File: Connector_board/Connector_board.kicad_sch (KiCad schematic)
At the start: 7 parts, among them J1 SM03B-SRSS-TB, J2 USB_B_Micro, J3 Conn_02x07_Counter_Clockwise, J4 Conn_02x07_Odd_Even, J5 Conn_02x07_Counter_Clockwise

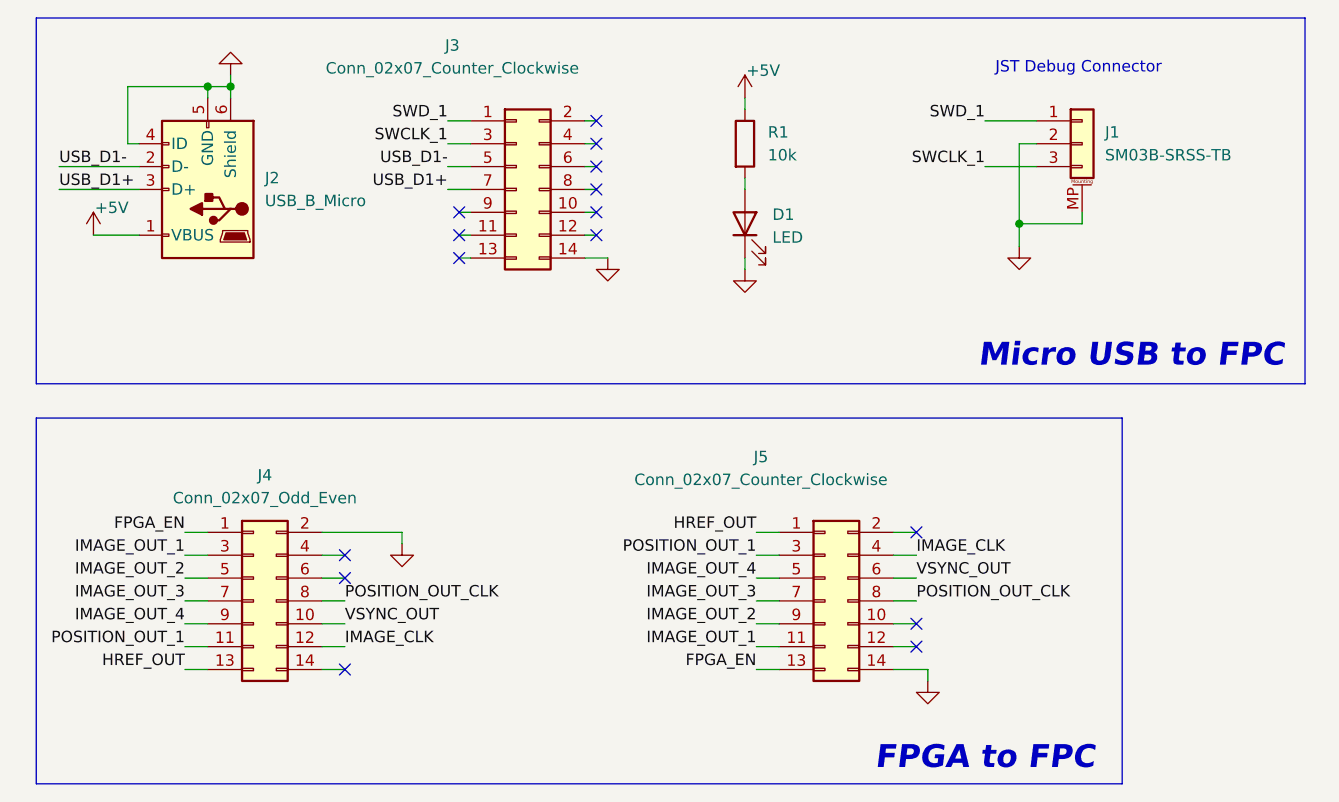
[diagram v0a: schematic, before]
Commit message: GPIO_1 added
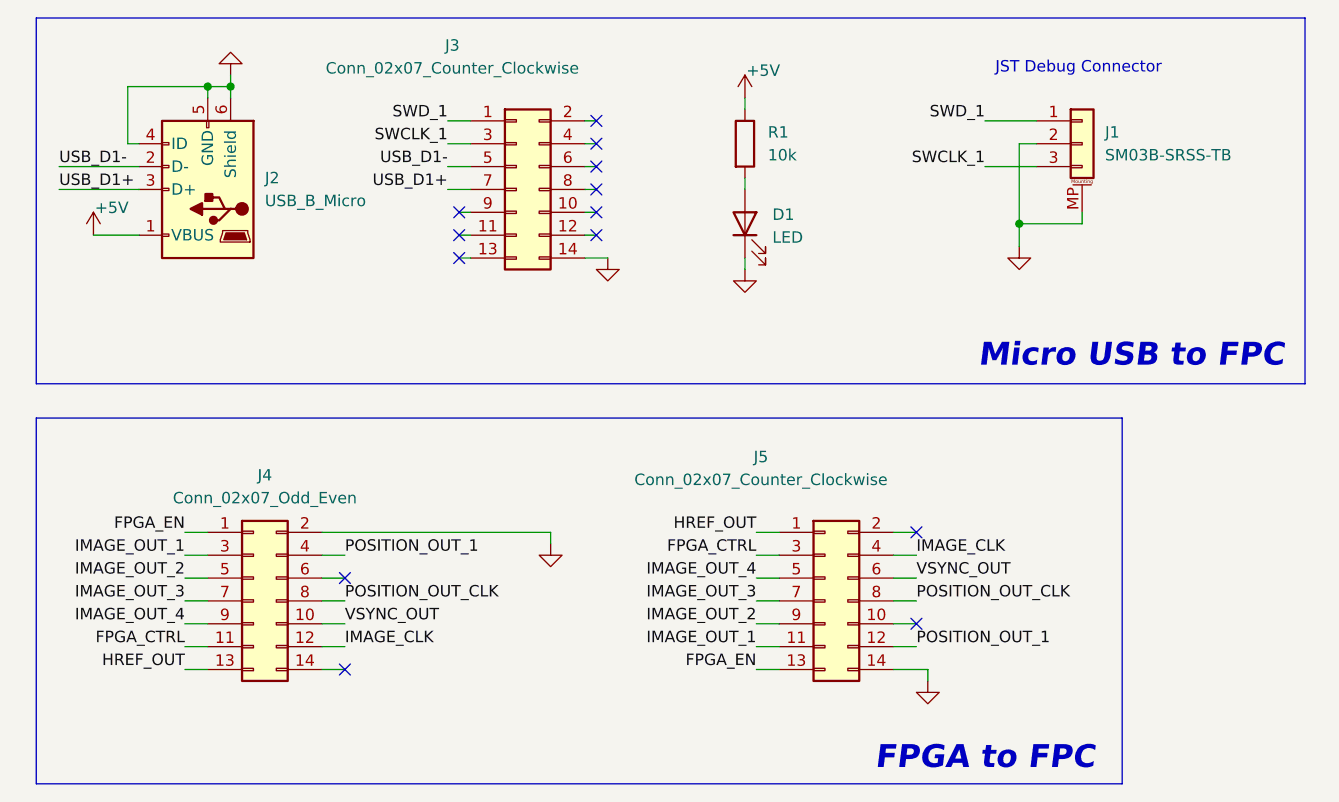
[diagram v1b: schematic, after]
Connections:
- net POSITION_OUT_1: now also J4.4 (Pin_4), J5.12 (Pin_12); no longer J4.11 (Pin_11), J5.3 (Pin_3)
- new net FPGA_CTRL: J4.11 (Pin_11), J5.3 (Pin_3)
- no-connect marks 15 -> 13
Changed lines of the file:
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@@
-	)
-	(no_connect
-		(at 111.76 83.82)
 	)
 	(no_connect
 		(at 60.96 35.56)
 	)
-	(no_connect
-		(at 48.26 73.66)
-	)
 	(wire
 		(pts
@@
 	(wire
 		(pts
-			(xy 45.72 71.12) (xy 54.61 71.12)
+			(xy 45.72 71.12) (xy 71.12 71.12)
 		)
 		(stroke
@@
 	(wire
 		(pts
-			(xy 54.61 72.39) (xy 54.61 71.12)
+			(xy 71.12 72.39) (xy 71.12 71.12)
 		)
 		(stroke
@@
 	)
 	(label "POSITION_OUT_1"
-		(at 30.48 83.82 180)
-		(effects
-			(font
-				(size 1.27 1.27)
-			)
-			(justify right bottom)
+		(at 111.76 83.82 0)
+		(effects
+			(font
+				(size 1.27 1.27)
+			)
+			(justify left bottom)
 		)
 	)
@@
 		)
 	)
+	(label "FPGA_CTRL"
+		(at 93.98 73.66 180)
+		(effects
+			(font
+				(size 1.27 1.27)
+			)
+			(justify right bottom)
+		)
+	)
+	(label "FPGA_CTRL"
+		(at 30.48 83.82 180)
+		(effects
+			(font
+				(size 1.27 1.27)
+			)
+			(justify right bottom)
+		)
+	)
 	(label "SWD_1"
 		(at 59.69 25.4 180)
@@
 		)
 	)
+	(label "POSITION_OUT_1"
+		(at 48.26 73.66 0)
+		(effects
+			(font
+				(size 1.27 1.27)
+			)
+			(justify left bottom)
+		)
+	)
 	(label "FPGA_EN"
 		(at 30.48 71.12 180)
@@
 	(label "IMAGE_OUT_3"
 		(at 93.98 78.74 180)
-		(effects
-			(font
-				(size 1.27 1.27)
-			)
-			(justify right bottom)
-		)
-	)
-	(label "POSITION_OUT_1"
-		(at 93.98 73.66 180)
 		(effects
 			(font
@@
 		(lib_name "GND_8")
 		(lib_id "power:GND")
-		(at 54.61 72.39 0)
+		(at 71.12 72.39 0)
 		(unit 1)
 		(body_style 1)
@@
 		(dnp no)
 		(property "Reference" "#PWR08"
-			(at 54.61 78.74 0)
+			(at 71.12 78.74 0)
 			(hide yes)
 			(show_name no)
@@
 		)
 		(property "Value" "GND"
-			(at 54.61 76.454 0)
+			(at 71.12 76.454 0)
 			(hide yes)
 			(show_name no)
@@
 		)
 		(property "Footprint" ""
-			(at 54.61 72.39 0)
+			(at 71.12 72.39 0)
 			(hide yes)
 			(show_name no)
@@
 		)
 		(property "Datasheet" ""
-			(at 54.61 72.39 0)
+			(at 71.12 72.39 0)
 			(hide yes)
 			(show_name no)
@@
 		)
 		(property "Description" "Power symbol creates a global label with name \"GND\" , ground"
-			(at 54.61 72.39 0)
-			(hide yes)
-			(show_name no)
+			(at 71.12 72.39 0)
+			(hide yes)
+			(show_name no)

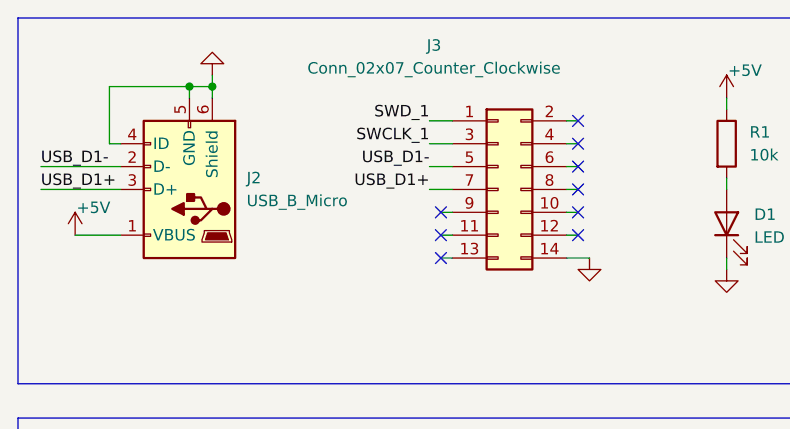
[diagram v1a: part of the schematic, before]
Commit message: connector board pin order updated
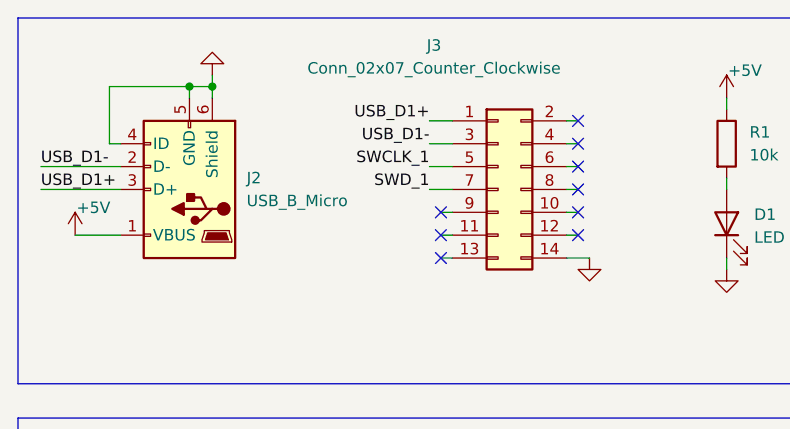
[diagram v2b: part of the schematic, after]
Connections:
- net SWCLK_1: now also J3.5 (Pin_5); no longer J3.3 (Pin_3)
- net SWD_1: now also J3.7 (Pin_7); no longer J3.1 (Pin_1)
- net USB_D1+: now also J3.1 (Pin_1); no longer J3.7 (Pin_7)
- net USB_D1-: now also J3.3 (Pin_3); no longer J3.5 (Pin_5)
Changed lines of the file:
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@@
+		)
+	)
+	(label "USB_D1+"
+		(at 59.69 25.4 180)
+		(effects
+			(font
+				(size 1.27 1.27)
+			)
+			(justify right bottom)
 		)
 	)
@@
 		)
 	)
-	(label "SWD_1"
-		(at 59.69 25.4 180)
-		(effects
-			(font
-				(size 1.27 1.27)
-			)
-			(justify right bottom)
-		)
-	)
 	(label "HREF_OUT"
 		(at 30.48 86.36 180)
@@
 			)
 			(justify left bottom)
+		)
+	)
+	(label "SWD_1"
+		(at 59.69 33.02 180)
+		(effects
+			(font
+				(size 1.27 1.27)
+			)
+			(justify right bottom)
 		)
 	)
@@
 		)
 	)
-	(label "USB_D1+"
-		(at 59.69 33.02 180)
-		(effects
-			(font
-				(size 1.27 1.27)
-			)
-			(justify right bottom)
-		)
-	)
 	(label "IMAGE_OUT_1"
 		(at 30.48 73.66 180)
@@
 	(label "FPGA_EN"
 		(at 93.98 86.36 180)
+		(effects
+			(font
+				(size 1.27 1.27)
+			)
+			(justify right bottom)
+		)
+	)
+	(label "USB_D1-"
+		(at 59.69 27.94 180)
 		(effects
 			(font
@@
 	)
 	(label "SWCLK_1"
-		(at 59.69 27.94 180)
-		(effects
-			(font
-				(size 1.27 1.27)
-			)
-			(justify right bottom)
-		)
-	)
-	(label "USB_D1-"
 		(at 59.69 30.48 180)
 		(effects

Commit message: new connector footprint updated
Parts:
- removed J3, J5: Conn_02x07_Counter_Clockwise, Connector_Molex:Molex_SlimStack_502430-1410_2x07_P0.40mm_Vertical, symbol Connector_Generic:Conn_02x07_Odd_Even
- removed J4: Conn_02x07_Odd_Even, Connector_PinHeader_2.54mm:PinHeader_2x07_P2.54mm_Vertical, symbol Connector_Generic:Conn_02x07_Odd_Even
- added J3: Conn_02x06_Odd_Even, Connector_PinHeader_2.54mm:PinHeader_2x06_P2.54mm_Vertical, symbol Connector_Generic:Conn_02x06_Odd_Even
- added J5, J6: Conn_02x06_Top_Bottom, 5035521222:CON_5035521222, symbol Connector_Generic:Conn_02x06_Top_Bottom
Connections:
- net FPGA_CTRL: now also J3.12 (Pin_12), J5.1 (Pin_1)
- net FPGA_EN: now also J3.2 (Pin_2), J5.6 (Pin_6)
- net GND: now also J3.1 (Pin_1), J5.12 (Pin_12), J6.12 (Pin_12)
- net HREF_OUT: now also J3.11 (Pin_11), J5.7 (Pin_7)
- net IMAGE_CLK: now also J3.9 (Pin_9), J5.8 (Pin_8)
- net IMAGE_OUT_1: now also J3.4 (Pin_4), J5.5 (Pin_5)
- net IMAGE_OUT_2: now also J3.6 (Pin_6), J5.4 (Pin_4)
- net IMAGE_OUT_3: now also J3.8 (Pin_8), J5.3 (Pin_3)
- net IMAGE_OUT_4: now also J3.10 (Pin_10), J5.2 (Pin_2)
- net POSITION_OUT_1: now also J3.3 (Pin_3), J5.11 (Pin_11)
- net POSITION_OUT_CLK: now also J3.5 (Pin_5), J5.10 (Pin_10)
- net SWCLK_1: now also J6.3 (Pin_3)
- net SWD_1: now also J6.4 (Pin_4)
- net USB_D1+: now also J6.1 (Pin_1)
- net USB_D1-: now also J6.2 (Pin_2)
- net VSYNC_OUT: now also J3.7 (Pin_7), J5.9 (Pin_9)
- no-connect marks 13 -> 7

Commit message: connector footprint swapped
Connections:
- net FPGA_CTRL: now also J5.7 (Pin_7); no longer J5.1 (Pin_1)
- net FPGA_EN: now also J5.12 (Pin_12); no longer J5.6 (Pin_6)
- net GND: now also J5.6 (Pin_6), J6.6 (Pin_6); no longer J5.12 (Pin_12), J6.12 (Pin_12)
- net HREF_OUT: now also J5.1 (Pin_1); no longer J5.7 (Pin_7)
- net IMAGE_CLK: now also J5.2 (Pin_2); no longer J5.8 (Pin_8)
- net IMAGE_OUT_1: now also J5.11 (Pin_11); no longer J5.5 (Pin_5)
- net IMAGE_OUT_2: now also J5.10 (Pin_10); no longer J5.4 (Pin_4)
- net IMAGE_OUT_3: now also J5.9 (Pin_9); no longer J5.3 (Pin_3)
- net IMAGE_OUT_4: now also J5.8 (Pin_8); no longer J5.2 (Pin_2)
- net POSITION_OUT_1: now also J5.5 (Pin_5); no longer J5.11 (Pin_11)
- net POSITION_OUT_CLK: now also J5.4 (Pin_4); no longer J5.10 (Pin_10)
- net SWCLK_1: now also J6.9 (Pin_9); no longer J6.3 (Pin_3)
- net SWD_1: now also J6.10 (Pin_10); no longer J6.4 (Pin_4)
- net USB_D1+: now also J6.7 (Pin_7); no longer J6.1 (Pin_1)
- net USB_D1-: now also J6.8 (Pin_8); no longer J6.2 (Pin_2)
- net VSYNC_OUT: now also J5.3 (Pin_3); no longer J5.9 (Pin_9)
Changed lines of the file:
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@@
 	(symbol
 		(lib_id "Connector_Generic:Conn_02x06_Top_Bottom")
-		(at 101.6 78.74 0)
-		(unit 1)
-		(body_style 1)
-		(exclude_from_sim no)
-		(in_bom yes)
-		(on_board yes)
-		(in_pos_files yes)
-		(dnp no)
-		(fields_autoplaced yes)
-		(property "Reference" "J5"
-			(at 102.87 67.31 0)
+		(at 69.85 30.48 0)
+		(mirror y)
+		(unit 1)
+		(body_style 1)
+		(exclude_from_sim no)
+		(in_bom yes)
+		(on_board yes)
+		(in_pos_files yes)
+		(dnp no)
+		(property "Reference" "J6"
+			(at 68.58 19.05 0)
 			(show_name no)
 			(do_not_autoplace no)
@@
 		)
 		(property "Value" "Conn_02x06_Top_Bottom"
-			(at 102.87 69.85 0)
+			(at 68.58 21.59 0)
 			(show_name no)
 			(do_not_autoplace no)
@@
 		)
 		(property "Footprint" "5035521222:CON_5035521222"
-			(at 101.6 78.74 0)
-			(hide yes)
-			(show_name no)
-			(do_not_autoplace no)
-			(effects
-				(font
-					(size 1.27 1.27)
-				)
-			)
-		)
-		(property "Datasheet" ""
-			(at 101.6 78.74 0)
+			(at 69.85 30.48 0)
+			(hide yes)
+			(show_name no)
+			(do_not_autoplace no)
+			(effects
+				(font
+					(size 1.27 1.27)
+				)
+			)
+		)
+		(property "Datasheet" ""
+			(at 69.85 30.48 0)
 			(hide yes)
 			(show_name no)
@@
 		)
 		(property "Description" "Generic connector, double row, 02x06, top/bottom pin numbering scheme (row 1: 1...pins_per_row, row2: pins_per_row+1 ... num_pins), script generated (kicad-library-utils/schlib/autogen/connector/)"
-			(at 101.6 78.74 0)
+			(at 69.85 30.48 0)
 			(hide yes)
 			(show_name no)
@@
 			(project "Connector_board"
 				(path "/d47a3cbb-9124-4e72-898a-608406011dc9"
-					(reference "J5")
+					(reference "J6")
 					(unit 1)
 				)
@@
 	)
 	(symbol
-		(lib_id "Connector_Generic:Conn_02x06_Top_Bottom")
-		(at 67.31 30.48 0)
-		(unit 1)
-		(body_style 1)
-		(exclude_from_sim no)
-		(in_bom yes)
-		(on_board yes)
-		(in_pos_files yes)
-		(dnp no)
-		(fields_autoplaced yes)
-		(property "Reference" "J6"
-			(at 68.58 19.05 0)
-			(show_name no)
-			(do_not_autoplace no)
-			(effects
-				(font
-					(size 1.27 1.27)
-				)
-			)
-		)
-		(property "Value" "Conn_02x06_Top_Bottom"
-			(at 68.58 21.59 0)
-			(show_name no)
-			(do_not_autoplace no)
-			(effects
-				(font
-					(size 1.27 1.27)
-				)
-			)
-		)
-		(property "Footprint" "5035521222:CON_5035521222"
-			(at 67.31 30.48 0)
-			(hide yes)
-			(show_name no)
-			(do_not_autoplace no)
-			(effects
-				(font
-					(size 1.27 1.27)
-				)
-			)
-		)
-		(property "Datasheet" ""
-			(at 67.31 30.48 0)
-			(hide yes)
-			(show_name no)
-			(do_not_autoplace no)
-			(effects
-				(font
-					(size 1.27 1.27)
-				)
-			)
-		)
-		(property "Description" "Generic connector, double row, 02x06, top/bottom pin numbering scheme (row 1: 1...pins_per_row, row2: pins_per_row+1 ... num_pins), script generated (kicad-library-utils/schlib/autogen/connector/)"
-			(at 67.31 30.48 0)
-			(hide yes)
-			(show_name no)
-			(do_not_autoplace no)
-			(effects
-				(font
-					(size 1.27 1.27)
-				)
-			)
-		)
-		(pin "11"
-		)
-		(pin "12"
-		)
-		(pin "3"
-		)
-		(pin "10"
-		)
-		(pin "7"
-		)
-		(pin "2"
-		)
-		(pin "9"
-		)
-		(pin "1"
-		)
-		(pin "4"
-		)
-		(pin "5"
-		)
-		(pin "8"
-		)
-		(pin "6"
-		)
-		(instances
-			(project "Connector_board"
-				(path "/d47a3cbb-9124-4e72-898a-608406011dc9"
-					(reference "J6")
-					(unit 1)
-				)
-			)
-		)
-	)
-	(symbol
 		(lib_id "Device:R")
 		(at 92.71 27.94 0)
@@
 					(unit 1)
 				)
+			)
+		)
+	)
+	(symbol
+		(lib_id "Connector_Generic:Conn_02x06_Top_Bottom")
+		(at 104.14 78.74 0)
+		(mirror y)
+		(unit 1)
+		(body_style 1)
+		(exclude_from_sim no)
+		(in_bom yes)
+		(on_board yes)
+		(in_pos_files yes)
+		(dnp no)
+		(property "Reference" "J5"
+			(at 102.87 67.31 0)
+			(show_name no)
+			(do_not_autoplace no)
+			(effects
+				(font
+					(size 1.27 1.27)
+				)
+			)
+		)
+		(property "Value" "Conn_02x06_Top_Bottom"
+			(at 102.87 69.85 0)
+			(show_name no)
+			(do_not_autoplace no)
+			(effects
+				(font
+					(size 1.27 1.27)
+				)
+			)
+		)
+		(property "Footprint" "5035521222:CON_5035521222"
+			(at 104.14 78.74 0)
+			(hide yes)
+			(show_name no)
+			(do_not_autoplace no)
+			(effects
+				(font
+					(size 1.27 1.27)
+				)
+			)
+		)
+		(property "Datasheet" ""
+			(at 104.14 78.74 0)
+			(hide yes)
+			(show_name no)
+			(do_not_autoplace no)
+			(effects
+				(font
+					(size 1.27 1.27)
+				)
+			)
+		)
+		(property "Description" "Generic connector, double row, 02x06, top/bottom pin numbering scheme (row 1: 1...pins_per_row, row2: pins_per_row+1 ... num_pins), script generated (kicad-library-utils/schlib/autogen/connector/)"
+			(at 104.14 78.74 0)
+			(hide yes)
+			(show_name no)
+			(do_not_autoplace no)
+			(effects
+				(font
+					(size 1.27 1.27)
+				)
+			)
+		)
+		(pin "11"
+		)
+		(pin "12"
+		)
+		(pin "3"
+		)
+		(pin "10"
+		)
+		(pin "7"
+		)
+		(pin "2"
+		)
+		(pin "9"
+		)
+		(pin "1"
+		)
+		(pin "4"
+		)
+		(pin "5"
+		)
+		(pin "8"
+		)
+		(pin "6"
+		)
+		(instances
+			(project "Connector_board"
+				(path "/d47a3cbb-9124-4e72-898a-608406011dc9"
+					(reference "J5")
+					(unit 1)
+				)
